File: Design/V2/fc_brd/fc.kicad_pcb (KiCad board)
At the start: 4 copper layers, 70.8 x 100 mm, 98 parts, among them J1 MCU Power, J2 Left Side Servo Power, J3 Right Side Servo Power, U1 STM32H747BIT6, U6 LD39200PU33R

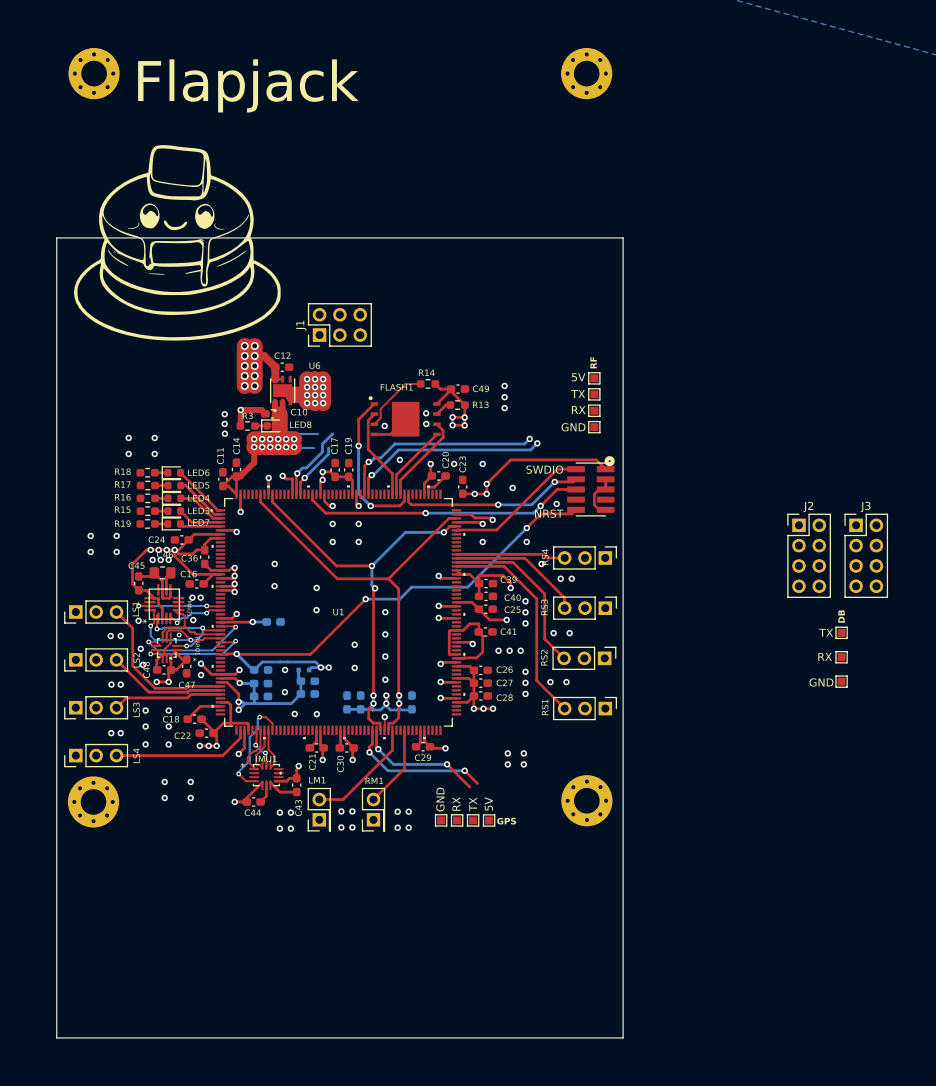
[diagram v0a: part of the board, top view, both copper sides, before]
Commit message: layout changed to main fc board
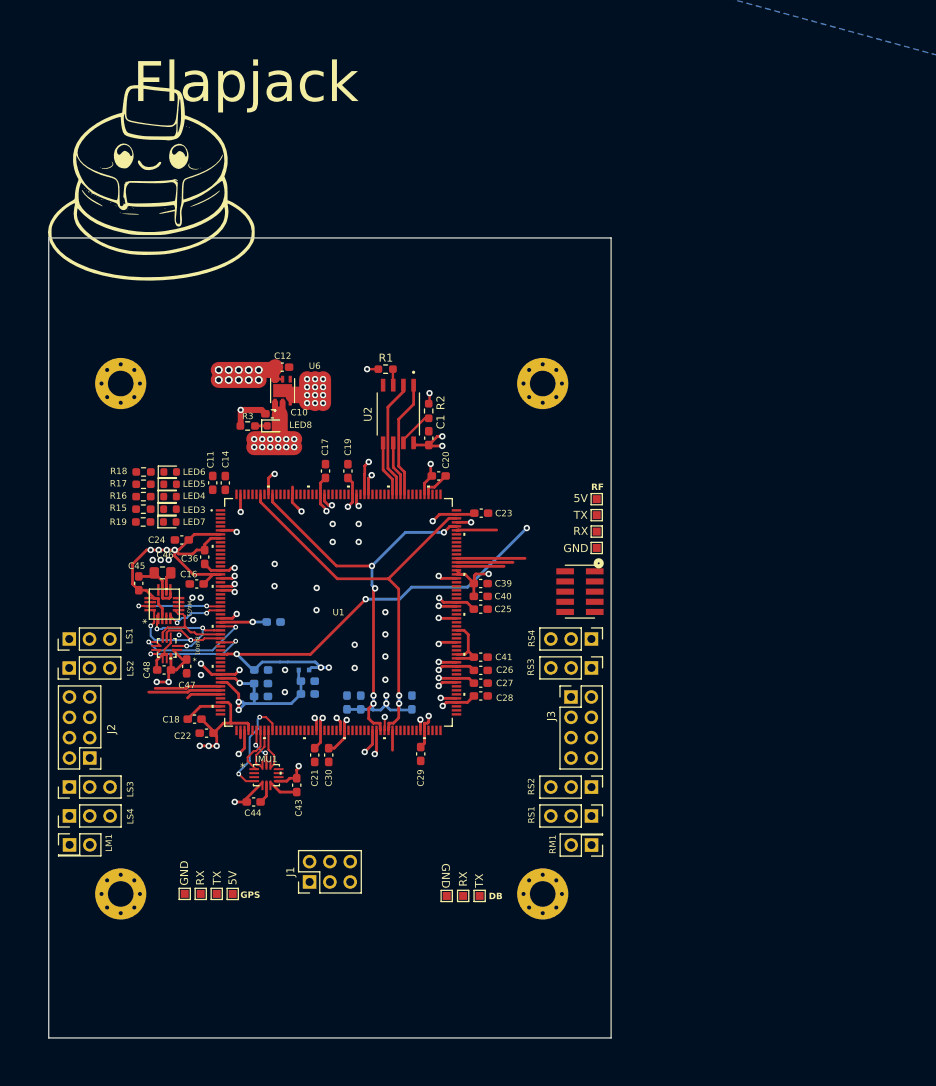
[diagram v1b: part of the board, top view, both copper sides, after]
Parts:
- removed C49: 100nF, Capacitor_SMD:C_0603_1608Metric_Pad1.08x0.95mm_HandSolder
- removed FLASH1: W25N01GWZEIG, Lib:W25N01GWZEIG
- removed R13, R14: 10K, Resistor_SMD:R_0603_1608Metric_Pad0.98x0.95mm_HandSolder
- added C1: 100nF, Capacitor_SMD:C_0603_1608Metric_Pad1.08x0.95mm_HandSolder, F.Cu at (209.5, 101.0)
- added R1: 10k, Resistor_SMD:R_0603_1608Metric_Pad0.98x0.95mm_HandSolder, F.Cu at (204.1, 92.4)
- added R2: 10k, Resistor_SMD:R_0603_1608Metric_Pad0.98x0.95mm_HandSolder, F.Cu at (209.5, 97.6)
- added U2: W25Q128JVSIQ, EXT_Storage:SOIC127P790X216-8N, F.Cu at (205.7, 98.0)
- moved J2 93.3 mm to (167.1, 141.0), turned to 180 degrees
- moved J1 68.4 mm to (194.6, 156.5)
- moved GND 56.2 mm to (211.8, 158.2), turned to -90 degrees
- moved TX 55.9 mm to (215.9, 158.2), turned to -90 degrees
- moved RX 55.9 mm to (213.8, 158.2), turned to -90 degrees
- moved J3 41.6 mm to (227.3, 133.4)
- moved H4 39.1 mm to (223.8, 94.2)
- moved H1 38.9 mm to (171.0, 94.2)
- moved 5V 33.3 mm to (185.0, 158.0)
- moved GND 33.3 mm to (179.0, 158.0)
- moved RX 33.3 mm to (181.0, 158.0)
- moved TX 33.3 mm to (183.0, 158.0)
- moved LM1 31.4 mm to (164.6, 151.9), turned to 0 degrees
- moved RM1 27.4 mm to (229.9, 151.9), turned to 180 degrees
- moved RS2 16.2 mm to (229.8, 144.6)
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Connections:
- J2 pad 1: SERVO_VCC_1_2 -> SERVO_VCC_3_4
- J2 pad 3: SERVO_VCC_1_2 -> SERVO_VCC_3_4
- J2 pad 5: SERVO_VCC_3_4 -> SERVO_VCC_1_2
- J2 pad 7: SERVO_VCC_3_4 -> SERVO_VCC_1_2
- LS1 pad 2: +5V -> SERVO_VCC_1_2
- LS2 pad 2: +5V -> SERVO_VCC_1_2
- LS3 pad 2: +5V -> SERVO_VCC_3_4
- LS4 pad 2: +5V -> SERVO_VCC_3_4
- RS1 pad 2: +5V -> SERVO_VCC_5_6
- RS2 pad 2: +5V -> SERVO_VCC_5_6
- RS3 pad 2: +5V -> SERVO_VCC_7_8
- RS4 pad 2: +5V -> SERVO_VCC_7_8
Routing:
- net +3.3V: track 213.6 -> 166.1 mm, vias 47 -> 44
- net DEBUG_SWO: track 35.6 -> 0.00 mm, vias 2 -> 0
- net DEBUG_SWCLK: track 23.4 -> 0.00 mm, vias 2 -> 0
- net RF_RECV_TX: track 24.9 -> 2.79 mm, vias 2 -> 1
- net RF_RECV_RX: track 25.6 -> 4.52 mm, vias 2 -> 1
- net R_SERVO_1_SIGNAL: track 26.9 -> 5.96 mm
- net GND: track 120.7 -> 104.2 mm, vias 137 -> 63
- net L_SERVO_4_SIGNAL: track 17.4 -> 1.01 mm
- net GPS_TX: track 18.0 -> 3.10 mm, vias 2 -> 1
- net R_SERVO_2_SIGNAL: track 21.7 -> 7.08 mm
- net R_SERVO_4_SIGNAL: track 13.7 -> 0.00 mm
- net DEBUG_SWDIO: track 18.1 -> 5.04 mm
- net GPS_RX: track 15.9 -> 3.05 mm, vias 2 -> 1
- net L_MOTOR_1_SIGNAL: track 14.2 -> 2.48 mm
- net L_SERVO_1_SIGNAL: track 19.8 -> 8.28 mm
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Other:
- board size 70.8 x 100 mm -> 70.3 x 100 mm
- board text removed: "GND +5V PWM"
- board text removed: "GND PWM"
- board text removed: "NRST"
- board text removed: "PWM +5V GND"
- board text removed: "SWDIO"
- board text removed: "TX RX GND"

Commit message: completed main fc board layout
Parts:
- added NT2: NT, Lib:NetTie-2_SMD_Track0.35mm, F.Cu at (211.4, 113.8)
- C13, C15, C31, C32, C34, C35, C37, C38, C42, NT1, NT2, NT5, NT7: moved to F.Cu
- FB1: footprint Lib:MPZ1005S121HT000 -> Inductor_SMD:L_0603_1608Metric_Pad1.05x0.95mm_HandSolder; moved to F.Cu
- G***: moved to B.Cu
- moved G*** 60.7 mm to (196.8, 125.6), turned to 180 degrees
- moved C34 27.3 mm to (217.0, 112.0), turned to 0 degrees
- moved C13 16.0 mm to (178.6, 134.0), turned to 180 degrees
- moved C32 16.0 mm to (178.6, 135.6), turned to 180 degrees
- moved FB1 15.5 mm to (178.6, 132.4), turned to 0 degrees
- moved C47 12.1 mm to (170.2, 121.4), turned to 180 degrees
- moved C15 10.9 mm to (180.5, 118.7), turned to 180 degrees
- moved C37 9.72 mm to (179.2, 130.6), turned to 180 degrees
- moved C38 9.71 mm to (179.2, 129.1), turned to 180 degrees
- moved C48 9.36 mm to (170.2, 123.0)
- moved C35 9.24 mm to (203.4, 142.3), turned to -90 degrees
- moved C31 8.62 mm to (205.0, 142.3), turned to -90 degrees
- moved C42 8.36 mm to (180.6, 127.6), turned to 180 degrees
- moved C46 8.25 mm to (169.6, 113.0)
- moved NT5 6.99 mm to (181.1, 131.4)
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- renumbered GND to TP1, RX to TP10, GND to TP12, RX to TP2, TX to TP3, 5V to TP4, TX to TP5, RX to TP6, 5V to TP7, GND to TP8, TX to TP9, BARO1 to U7, MAG1 to U8, IMU1 to U9
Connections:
- RS1 pad 2: SERVO_VCC_5_6 -> SERVO_VCC_7_8
- RS2 pad 2: SERVO_VCC_5_6 -> SERVO_VCC_7_8
- RS3 pad 2: SERVO_VCC_7_8 -> SERVO_VCC_5_6
- RS4 pad 2: SERVO_VCC_7_8 -> SERVO_VCC_5_6
- U1 pad 192: CURRENT_SENSE_SCL -> unconnected-(U1A-PB6-Pad192)
- U1 pad 193: CURRENT_SENSE_SDA -> unconnected-(U1A-PB7-Pad193)
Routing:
- net GND: track 104.2 -> 149.9 mm, vias 63 -> 113
- net L_MOTOR_1_SIGNAL: track 2.48 -> 45.5 mm, vias 0 -> 2
- net DEBUG_SWO: track 0.00 -> 37.4 mm, vias 0 -> 2
- net R_SERVO_1_SIGNAL: track 5.96 -> 38.5 mm
- net R_MOTOR_1_SIGNAL: track 0.00 -> 31.0 mm
- net R_SERVO_2_SIGNAL: track 7.08 -> 37.1 mm
- net RF_RECV_TX: track 2.79 -> 31.5 mm, vias 1 -> 2
- net RF_RECV_RX: track 4.52 -> 33.1 mm, vias 1 -> 2
- net GPS_TX: track 3.10 -> 30.5 mm, vias 1 -> 0
- net DEBUG_SWCLK: track 0.00 -> 27.0 mm, vias 0 -> 2
- net GPS_RX: track 3.05 -> 29.4 mm, vias 1 -> 0
- net DEBUG_RX: track 0.00 -> 23.0 mm, vias 0 -> 2
- net DEBUG_TX: track 0.00 -> 22.2 mm, vias 0 -> 2
- net R_SERVO_4_SIGNAL: track 0.00 -> 20.3 mm
- net L_SERVO_4_SIGNAL: track 1.01 -> 21.3 mm
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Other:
- board size 70.3 x 100 mm -> 70.3 x 73.2 mm
- board text added: "1&2 V G"
- board text added: "3&4 V G"
- board text added: "5V"
- board text added: "G V 5&6"
- board text added: "G V 7&8"
- board text added: "GND"
- board text added: "GND SIG"
- board text added: "GND SVCC SIG"
- board text added: "RX"
- board text added: "SIG GND"
- board text added: "SIG SVCC GND"
- board text added: "TX"

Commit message: fc and power board sent out for assembly
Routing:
- net +3.3V: track 185.5 -> 209.6 mm, vias 48 -> 47
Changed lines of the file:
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@@
 		(tags "capacitor handsolder")
 		(property "Reference" "C20"
-			(at 0.898934 -1.987345 270)
+			(at 3.05 0.05 0)
 			(layer "F.SilkS")
 			(effects
@@
 	)
 	(via
-		(at 212.6 98)
+		(at 212.4 100.2)
 		(size 1)
 		(drill 0.5)
@@
 	)
 	(via
-		(at 212.6 96.6)
+		(at 212.4 98.4)
 		(size 1)
 		(drill 0.5)
@@
 	)
 	(via
-		(at 212.6 99.4)
+		(at 212.4 102)
 		(size 1)
 		(drill 0.5)
@@
 	)
 	(segment
+		(start 214.4 102.2)
+		(end 214.4 98.4)
+		(width 0.35)
+		(layer "F.Cu")
+		(net 152)
+	)
+	(segment
 		(start 219.896648 116.496648)
 		(end 229.076648 116.496648)
@@
 	)
 	(segment
-		(start 210.592326 100.8)
-		(end 209.508578 101.883748)
+		(start 211.255982 103.619993)
+		(end 212.980007 103.619993)
 		(width 0.35)
 		(layer "F.Cu")
@@
 	)
 	(segment
+		(start 209.495995 96.716969)
+		(end 209.495995 94.802949)
+		(width 0.35)
+		(layer "F.Cu")
+		(net 152)
+	)
+	(segment
+		(start 212.716969 96.716969)
+		(end 209.495995 96.716969)
+		(width 0.35)
+		(layer "F.Cu")
+		(net 152)
+	)
+	(segment
 		(start 190.6875 102.8)
 		(end 190.879384 102.608116)
@@
 	)
 	(segment
+		(start 211.255982 103.619993)
+		(end 209.819993 103.619993)
+		(width 0.35)
+		(layer "F.Cu")
+		(net 152)
+	)
+	(segment
 		(start 186 134.8)
 		(end 186 134.499996)
@@
 	)
 	(segment
-		(start 209.62483 102)
-		(end 209.508578 101.883748)
-		(width 0.35)
-		(layer "F.Cu")
-		(net 152)
-	)
-	(segment
 		(start 181.2 123.2)
 		(end 182.049998 124.049998)
@@
 	)
 	(segment
-		(start 201.8 92.4)
-		(end 203.2 92.4)
-		(width 0.3)
-		(layer "F.Cu")
-		(net 152)
-	)
-	(segment
 		(start 208.971135 137.549994)
 		(end 208.971135 139.166365)
@@
 	)
 	(segment
+		(start 212.980007 103.619993)
+		(end 214.4 102.2)
+		(width 0.35)
+		(layer "F.Cu")
+		(net 152)
+	)
+	(segment
 		(start 206.3 136)
 		(end 206.4 136)
@@
 	)
 	(segment
-		(start 201.8 136)
-		(end 201.2 135.4)
+		(start 211.255982 103.619993)
+		(end 211.255982 103.455982)
+		(width 0.35)
+		(layer "F.Cu")
+		(net 152)
+	)
+	(segment
+		(start 209.819993 103.619993)
+		(end 209.8 103.6)
 		(width 0.35)
 		(layer "F.Cu")
@@
 	)
 	(segment
-		(start 211 102)
-		(end 209.62483 102)
+		(start 201.8 136)
+		(end 201.2 135.4)
 		(width 0.35)
 		(layer "F.Cu")
@@
 	)
 	(segment
+		(start 203.978 91.622)
+		(end 203.2 92.4)
+		(width 0.35)
+		(layer "F.Cu")
+		(net 152)
+	)
+	(segment
 		(start 210.8 121)
 		(end 211.349998 121.549998)
@@
 	)
 	(segment
+		(start 211.244823 103.619993)
+		(end 209.508578 101.883748)
+		(width 0.35)
+		(layer "F.Cu")
+		(net 152)
+	)
+	(segment
 		(start 185.6 110.4)
 		(end 185.471134 110.271134)
@@
 	)
 	(segment
+		(start 209.495995 94.802949)
+		(end 206.315046 91.622)
+		(width 0.35)
+		(layer "F.Cu")
+		(net 152)
+	)
+	(segment
 		(start 181.4 116.2)
 		(end 181.4 116.83416)
@@
 	)
 	(segment
+		(start 209.8 103.6)
+		(end 209.8 102.17517)
+		(width 0.35)
+		(layer "F.Cu")
+		(net 152)
+	)
+	(segment
 		(start 215.050003 110.549997)
 		(end 212.97113 110.549997)
@@
 	)
 	(segment
+		(start 211.255982 103.619993)
+		(end 211.244823 103.619993)
+		(width 0.35)
+		(layer "F.Cu")
+		(net 152)
+	)
+	(segment
 		(start 211.25 134.5)
 		(end 211.700002 134.049998)
@@
 	)
 	(segment
-		(start 209.600878 95.239472)
-		(end 209.6 95.24035)
-		(width 0.3)
-		(layer "F.Cu")
-		(net 152)
-	)
-	(segment
 		(start 211.700002 134.049998)
 		(end 212.97113 134.049998)
@@
 	)
 	(segment
+		(start 209.8 102.17517)
+		(end 209.508578 101.883748)
+		(width 0.35)
+		(layer "F.Cu")
+		(net 152)
+	)
+	(segment
 		(start 210.5 110.9)
 		(end 210.850003 110.549997)
@@
 	)
 	(segment
+		(start 214.4 98.4)
+		(end 212.716969 96.716969)
+		(width 0.35)
+		(layer "F.Cu")
+		(net 152)
+	)
+	(segment
 		(start 188.282784 98.625952)
 		(end 188.282784 100.482784)
@@
 	)
 	(segment
-		(start 211 100.8)
-		(end 210.592326 100.8)
-		(width 0.35)
-		(layer "F.Cu")
-		(net 152)
-	)
-	(segment
 		(start 199.25 136.25)
 		(end 198.971135 136.528865)
@@
 	)
 	(segment
+		(start 206.315046 91.622)
+		(end 203.978 91.622)
+		(width 0.35)
+		(layer "F.Cu")
+		(net 152)
+	)
+	(segment
 		(start 182.511065 107.486065)
 		(end 182.5 107.475)
@@
 	)
 	(segment
+		(start 208.4 103.6)
+		(end 209.8 103.6)
+		(width 0.35)
+		(layer "F.Cu")
+		(net 152)
+	)
+	(segment
 		(start 187.7375 145.042338)
 		(end 188.715435 144.064403)
@@
 		(net 152)
 	)
-	(segment
-		(start 209.6 95.24035)
-		(end 209.6 96.612964)
-		(width 0.3)
-		(layer "F.Cu")
-		(net 152)
-	)
 	(via
 		(at 188.6875 102.8)
@@
 	)
 	(via
-		(at 170 120.175508)
+		(at 211.255982 103.619993)
 		(size 0.8)
 		(drill 0.4)
@@
 	)
 	(via
-		(at 211.25 134.5)
+		(at 170 120.175508)
 		(size 0.8)
 		(drill 0.4)
@@
 	)
 	(via
-		(at 185.6 110.4)
+		(at 211.25 134.5)
 		(size 0.8)
 		(drill 0.4)
@@
 	)
 	(via
-		(at 187.6875 102.8)
+		(at 185.6 110.4)
 		(size 0.8)
 		(drill 0.4)
@@
 	)
 	(via
-		(at 201.8 92.4)
+		(at 187.6875 102.8)
 		(size 0.8)
 		(drill 0.4)
@@
 	)
 	(via
-		(at 211 100.8)
+		(at 208.4 103.6)
 		(size 0.8)
 		(drill 0.4)
@@
 	)
 	(via
-		(at 209.600878 95.239472)
-		(size 0.8)
-		(drill 0.4)
-		(layers "F.Cu" "B.Cu")
-		(net 152)
-	)
-	(via
 		(at 199.25 136.25)
 		(size 0.8)
@@
 	)
 	(via
-		(at 211 102)
+		(at 209.8 103.6)
 		(size 0.8)
 		(drill 0.4)
@@
 		(net 152)
 		(net_name "+3.3V")
-		(locked yes)
 		(layer "In2.Cu")
 		(hatch edge 0.5)
@@
 		(polygon
 			(pts
-				(xy 200.8 90.6) (xy 199.445782 94.167228) (xy 196.75 97.75) (xy 174.242132 98.021179) (xy 167.4 118.4)
-				(xy 168 125.2) (xy 174.8 139) (xy 184.8 147.4) (xy 193.6 147.2) (xy 209.6 142.2) (xy 210.895752 141.252207)
-				(xy 215.511475 135.587455) (xy 218 134) (xy 218.6 128.4) (xy 219 116.621028) (xy 217.231881 106.424476)
-				(xy 215.847164 93.794178)
+				(xy 202 101.8) (xy 197.4 100.2) (xy 190.6 100.4) (xy 173.8 103) (xy 167.8 118.6) (xy 168 125.2)
+				(xy 174.8 139) (xy 184.8 147.4) (xy 193.6 147.2) (xy 209.6 142.2) (xy 210.895752 141.252207) (xy 215.511475 135.587455)
+				(xy 218 134) (xy 218.6 128.4) (xy 219 116.621028) (xy 217.231881 106.424476) (xy 212.8 102)
 			)
 		)

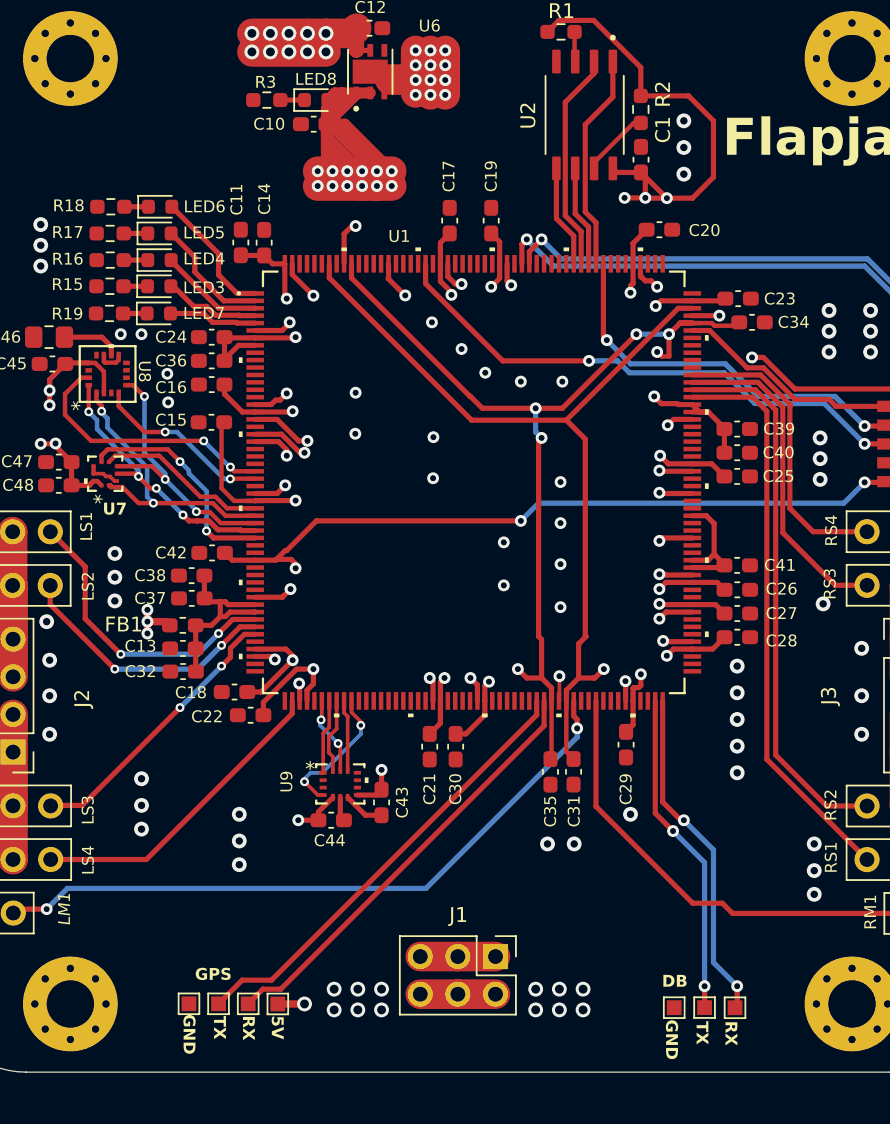
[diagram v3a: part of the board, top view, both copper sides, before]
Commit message: VCORE is regulated with LDO instead of SMPS. Remove VCAP connection to 3.3V as VCAP is an output not an input
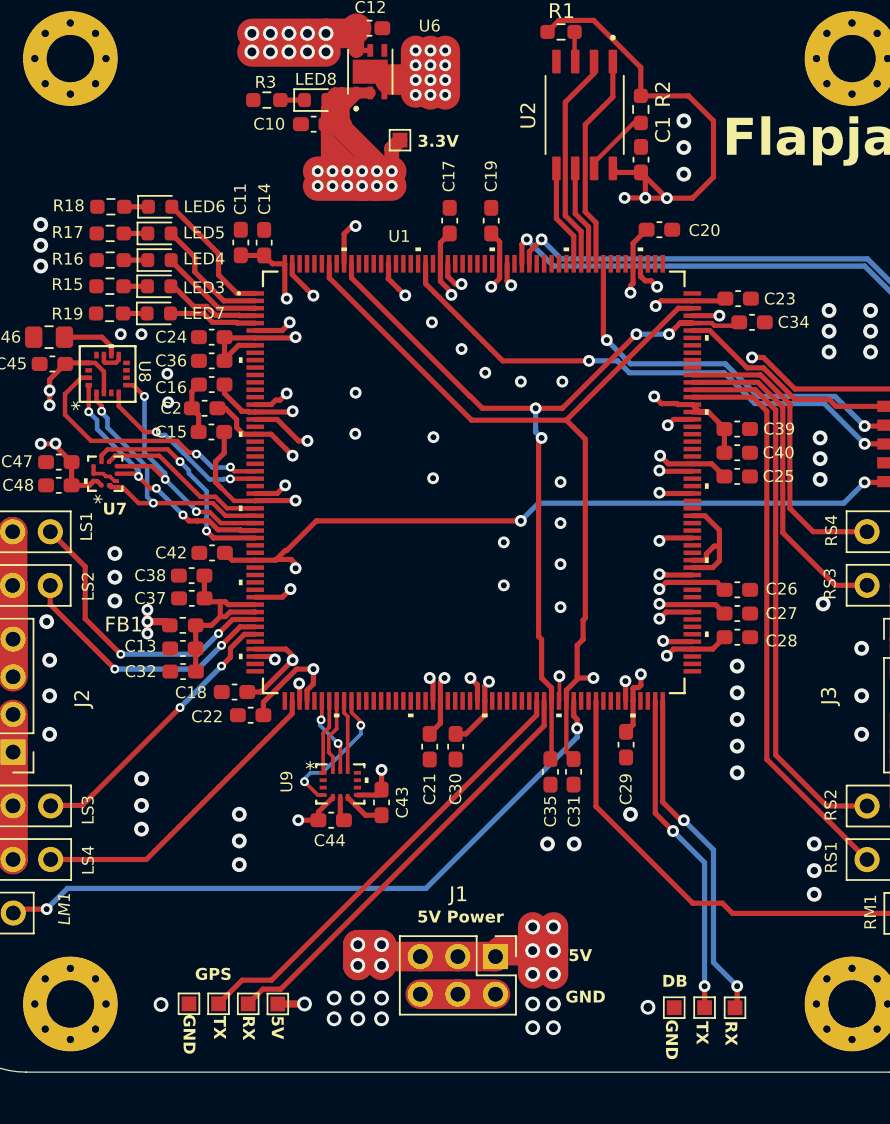
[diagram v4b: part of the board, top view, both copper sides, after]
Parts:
- removed C41: 2.2uF, Capacitor_SMD:C_0603_1608Metric_Pad1.08x0.95mm_HandSolder
- removed the NT2 at (202.3, 136.0)
- removed the NT2 at (211.4, 113.8)
- added C2: 4.7uF, Capacitor_SMD:C_0603_1608Metric_Pad1.08x0.95mm_HandSolder, F.Cu at (180.1, 117.8)
- added NT2: NT, Lib:NetTie-2_SMD_Track0.35mm, F.Cu at (185.2, 120.2)
- added TP7: TestPoint, TestPoint:TestPoint_Pad_1.0x1.0mm, F.Cu at (193.2, 99.7)
- R15, R16, R17, R18, R19, R3: value 39 -> 200
- moved C15 0.66 mm to (180.5, 119.4)
- moved NT3 0.40 mm to (214.8, 127.6), turned to -90 degrees
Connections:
- NT3 pad 1: /Power/VCAPDSI -> VDD12DSI
- NT3 pad 2: VDD12DSI -> /Power/VCAPDSI
- U1 pad 20: GND -> /Power/VDDSMPS
- U1 pad 21: GND -> unconnected-(U1D-VFBSDMPS-Pad21)
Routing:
- net +5V: track 24.4 -> 43.7 mm, vias 12 -> 22
- net /Power/VDDSMPS: track 0.00 -> 5.08 mm
- net GND: track 149.9 -> 146.8 mm, vias 113 -> 111
- net +3.3V: track 209.6 -> 210.6 mm, vias 47 -> 46
- net /Power/VCAP: track 59.0 -> 58.5 mm
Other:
- board text added: "3.3V"
- board text added: "5V Power"
